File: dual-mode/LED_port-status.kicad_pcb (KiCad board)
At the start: 2 copper layers, 23.7 x 12.5 mm, 21 parts, among them P1 CONN_9

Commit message: Tiny layout tweek.
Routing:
- net Net-(D16-Pad1): track 13.0 -> 12.3 mm

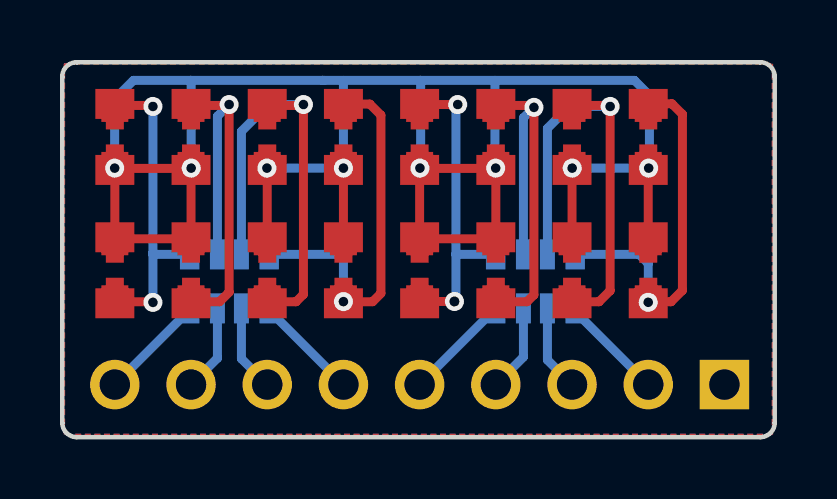
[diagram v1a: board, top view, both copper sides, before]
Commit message: Testing 0201 footprint. Some clearance issues.
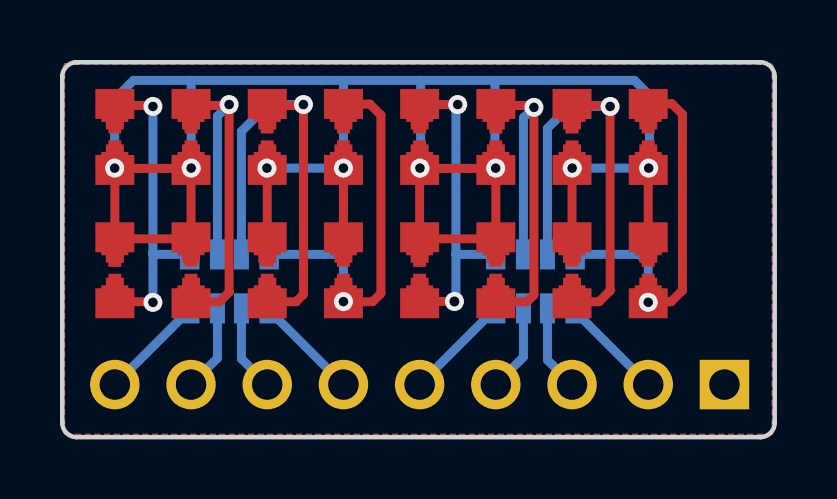
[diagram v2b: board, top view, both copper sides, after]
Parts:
- D1, D10, D11, D12, D13, D14, D15, D16, D2, D3, D4, D5, D6, D7, D8, D9: footprint my_parts:R_0805_0603_0402 -> my_parts:R_0805_0603_0402_0201
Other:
- board text added: "LED_port-status V0.21.c 2015 - blog.spitzenpfeil.org"
- board text removed: "LED_port-status V0.21.b 2015 - blog.spitzenpfeil.org"
